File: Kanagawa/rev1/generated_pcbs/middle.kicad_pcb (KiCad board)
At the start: 2 copper layers, 330 x 142 mm, 184 parts, among them J1 Conn_01x04, SW99 Rotary_Encoder_Switch, U0 Elite-C

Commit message: edit arc for edge cut in script
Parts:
- removed MountBaseMiddleTop7: MountingHole, keyboard:MountingHole_2.2mm_M2_Pad_Via
- J1: footprint keyboard:OLED_128x64_I2C -> keyboard:OLED_128x64_I2C_cutout
- RSW0: value SW_Push -> SW_RST
- moved RSW0 57.7 mm to (312.7, 78.2)
- moved R2 35.6 mm to (364.9, 79.6)
- moved R1 29.9 mm to (362.0, 80.9)
- moved DA13 18.6 mm to (368.9, 92.9)
- moved SW99 5.53 mm to (373.8, 104.6), turned to 90 degrees
- moved J1 4.21 mm to (331.9, 79.4)
- moved MountBaseMiddleTop1 2.40 mm to (60.0, 81.0)
- moved MountBaseMiddleTop5 2.23 mm to (381.0, 81.0)
- moved MountBaseMiddleTop3 2.00 mm to (244.9, 81.2)
- moved MountMiddle0 2.00 mm to (220.9, 83.2)
- moved MountBaseMiddleTop2 0.92 mm to (60.0, 207.0)
- moved MountBaseMiddleTop4 0.92 mm to (244.0, 207.0)
- moved MountBaseMiddleTop6 0.92 mm to (380.0, 207.0)
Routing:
- net ENCA: track 39.4 -> 14.4 mm
- net RESET: track 52.6 -> 71.1 mm
- net ENCB: track 41.8 -> 27.8 mm
- net col13: track 145.1 -> 153.3 mm
- net VCC: track 76.7 -> 69.8 mm, vias 1 -> 2
- net row00: track 416.4 -> 422.5 mm, vias 0 -> 1
- net SCL: track 78.9 -> 73.7 mm
- net SDA: track 69.4 -> 66.3 mm
- net /SW99B: track 8.86 -> 10.9 mm
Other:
- board size 330 x 142 mm -> 330 x 144 mm

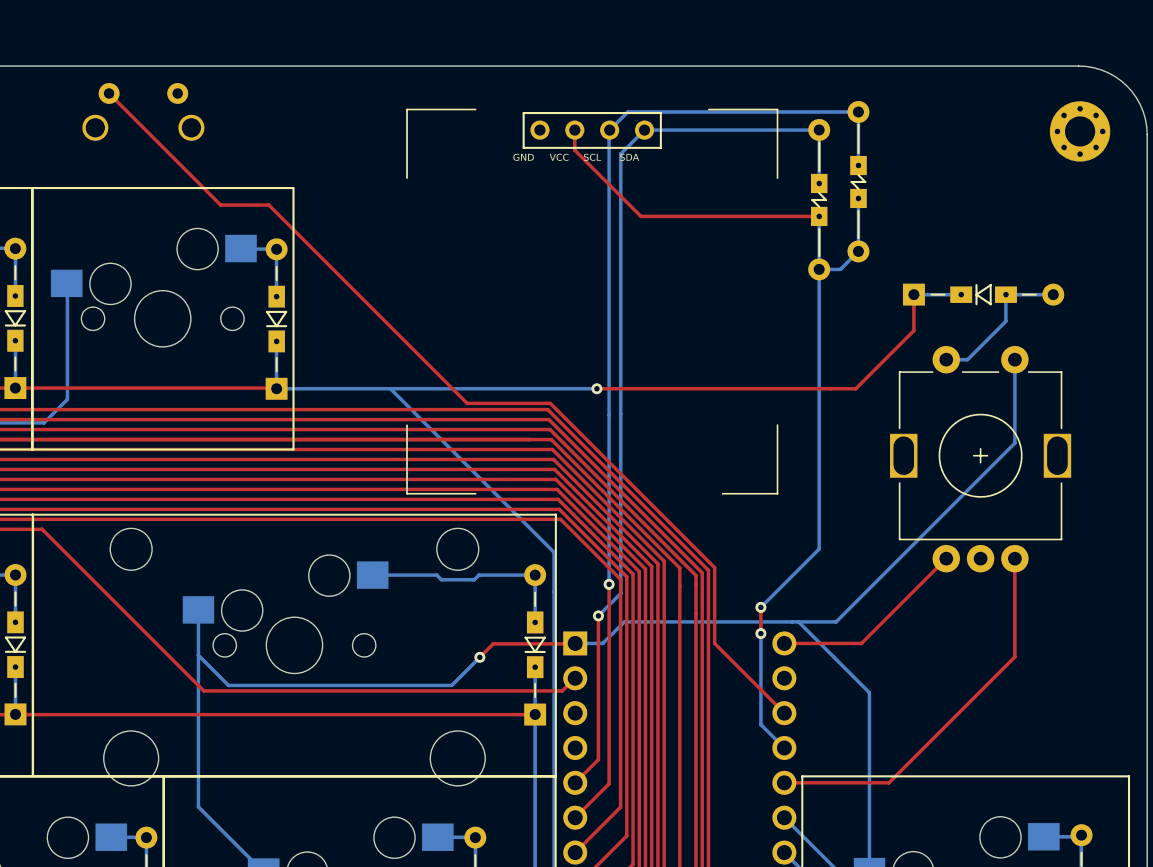
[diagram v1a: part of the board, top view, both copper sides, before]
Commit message: update script pcb generation
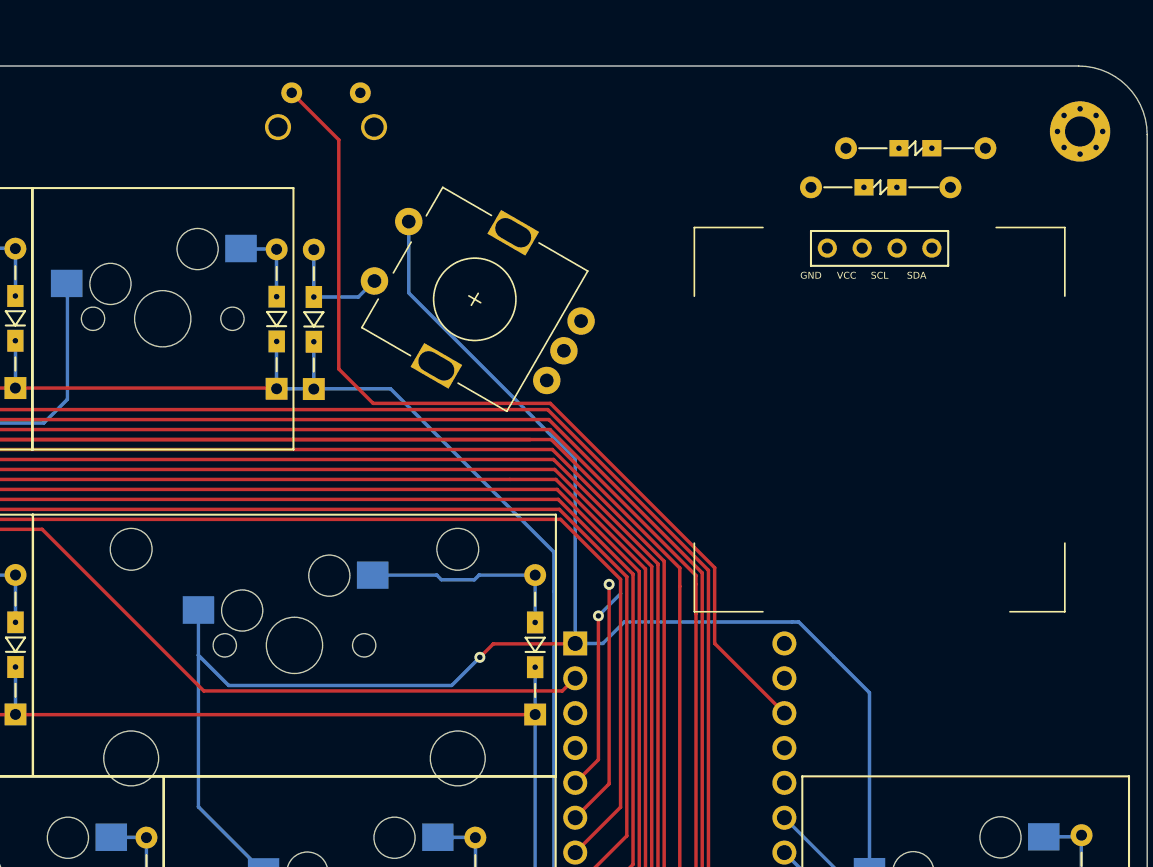
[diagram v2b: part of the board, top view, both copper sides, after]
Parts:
- moved DA13 44.3 mm to (325.2, 99.8), turned to 90 degrees
- moved SW99 38.6 mm to (336.9, 93.2), turned to 150 degrees
- moved J1 22.6 mm to (352.9, 88.0)
- moved RSW0 13.3 mm to (326.1, 78.2)
- moved R1 12.2 mm to (374.1, 82.2), turned to 180 degrees
- moved R2 8.66 mm to (371.6, 85.1), turned to 180 degrees
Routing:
- net VCC: track 69.8 -> 0.09 mm, vias 2 -> 0
- net SCL: track 73.7 -> 18.0 mm
- net SDA: track 66.3 -> 15.2 mm
- net row00: track 422.5 -> 380.0 mm, vias 1 -> 0
- net ENCB: track 27.8 -> 0.00 mm
- net ENCA: track 14.4 -> 0.00 mm
- net col13: track 153.3 -> 161.8 mm
- net RESET: track 71.1 -> 67.6 mm
- net /SW99B: track 10.9 -> 8.35 mm

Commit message: rework rev1 from fusion layout
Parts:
- added MountBaseMiddleTop3: MountingHole, keyboard:MountingHole_2.2mm_M2_Pad_Via, F.Cu at (125.9, 81.2)
- added MountBaseMiddleTop4: MountingHole, keyboard:MountingHole_2.2mm_M2_Pad_Via, F.Cu at (125.9, 207.2)
- DA0, DA1, DA10, DA11, DA12, DA13, DA2, DA3, DA4, DA5, DA6, DA7, DA8, DA9, DB0, DB1, DB10, DB11, DB12, DB13, DB2, DB3, DB4, DB5, DB6, DB7, DB8, DB9, DC0, DC1, DC10, DC11, DC12, DC13, DC2, DC3, DC4, DC5, DC6, DC7, DC8, DC9, DD0, DD1, DD10, DD11, DD12, DD13, DD2, DD3, DD4, DD5, DD6, DD7, DD8, DD9, DE0, DE1, DE10, DE11, DE12, DE13, DE2, DE3, DE4, DE5, DE6, DE7, DE8, DE9, DF0, DF1, DF10, DF11, DF12, DF13, DF2, DF3, DF4, DF5, DF6, DF7, DF8, DF9: footprint keyboard:Diode_SMD_THT -> keyboard:Diode_THT
- KD13, KE13, KF13: footprint keyboard:SW_Cherry_MX_1.25u_Hotswap -> keyboard:SW_Cherry_MX_1.00u_Hotswap
- R1, R2: footprint keyboard:Resistors_SMD_THT -> keyboard:Resistors_THT
- RSW0: value SW_RST -> SW_Push
- moved DA13 39.5 mm to (364.6, 103.2), turned to 0 degrees
- moved SW99 39.4 mm to (370.6, 113.5), turned to 90 degrees
- moved J1 22.9 mm to (331.6, 79.5)
- moved R1 17.8 mm to (364.3, 97.1), turned to 90 degrees
- moved R2 15.7 mm to (361.6, 97.1), turned to 90 degrees
- moved MountBaseMiddleTop7 4.12 mm to (376.9, 81.2)
- moved DE13 3.50 mm to (380.3, 164.9)
- moved DD13 3.48 mm to (380.3, 145.8)
- moved DF13 3.27 mm to (380.3, 184.0)
- moved MountBaseMiddleTop8 3.12 mm to (376.9, 207.2)
- moved LogoMiddle 2.83 mm to (374.9, 197.2)
- moved RSW0 2.00 mm to (324.1, 78.2)
- moved MountBaseMiddleTop1 1.90 mm to (61.9, 81.2)
- moved MountBaseMiddleTop2 1.90 mm to (61.9, 207.2)
- moved MountMiddle0 1.05 mm to (220.9, 82.2)
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- renumbered MountBaseMiddleTop3 to MountBaseMiddleTop5, MountBaseMiddleTop4 to MountBaseMiddleTop6, MountBaseMiddleTop5 to MountBaseMiddleTop7, MountBaseMiddleTop6 to MountBaseMiddleTop8
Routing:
- net VCC: track 0.09 -> 65.6 mm
- net row01: track 366.7 -> 318.3 mm
- net row02: track 353.3 -> 305.0 mm
- net SDA: track 15.2 -> 62.2 mm, vias 1 -> 2
- net row05: track 431.7 -> 386.1 mm
- net SCL: track 18.0 -> 63.5 mm, vias 1 -> 2
- net row03: track 367.3 -> 323.2 mm
- net row04: track 384.1 -> 340.3 mm
- net row00: track 380.0 -> 362.1 mm
- net ENCA: track 0.00 -> 9.82 mm, vias 0 -> 1
- net ENCB: track 0.00 -> 9.45 mm
- net col13: track 161.8 -> 155.0 mm
- net Net-(DD13-Pad2): track 6.04 -> 9.79 mm
- net Net-(DE13-Pad2): track 6.12 -> 9.79 mm
- net Net-(DF4-Pad2): track 15.5 -> 12.1 mm
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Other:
- board size 330 x 144 mm -> 325 x 143 mm

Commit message: review board
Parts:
- moved KD12 23.5 mm to (299.8, 147.3)
- moved KE0 23.4 mm to (56.9, 166.4)
- moved KF4 21.6 mm to (147.4, 190.8)
- moved KB13 21.3 mm to (304.5, 109.2)
- moved KF5 21.1 mm to (186.5, 200.6)
- moved KE11 19.2 mm to (290.3, 166.4)
- moved KD0 19.1 mm to (56.9, 147.3)
- moved KC13 17.2 mm to (314.1, 128.3)
- moved KC0 17.1 mm to (56.9, 128.3)
- moved KF2 15.2 mm to (99.8, 185.4)
- moved KF0 15.2 mm to (56.9, 185.4)
- moved KD13 13.7 mm to (381.9, 128.3)
- moved KE13 13.6 mm to (381.9, 147.3)
- moved KF13 13.6 mm to (381.9, 166.4)
- moved KA0 13.6 mm to (56.9, 85.1)
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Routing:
- net col03: track 602.9 -> 390.8 mm
- net ENCB: track 9.45 -> 19.6 mm
- net col07: track 324.4 -> 334.5 mm
- net col06: track 346.3 -> 356.4 mm
- net col08: track 303.5 -> 312.3 mm
- net col09: track 283.7 -> 290.4 mm
- net col05: track 366.8 -> 373.4 mm
- net col02: track 411.3 -> 415.6 mm
- net col01: track 441.3 -> 437.8 mm
- net col04: track 370.9 -> 372.9 mm
- net Net-(DD12-Pad2): track 14.4 -> 12.4 mm
- net col12: track 208.1 -> 209.7 mm
- net col11: track 249.9 -> 251.4 mm
- net row03: track 323.2 -> 321.7 mm
- net col13: track 155.0 -> 156.3 mm
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
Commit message: generate kanagawa gerber
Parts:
- moved RSW0 5.00 mm to (319.1, 78.2)
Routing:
- net RESET: track 68.5 -> 70.6 mm
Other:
- outline, holes or cut-outs redrawn
- board text added: "Kanagawa by Ciaanh - rev1"
- board text removed: "Kanagawa by Ciaanh - rev1 *prototype*"
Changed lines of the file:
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@@
-(kicad_pcb (version 20171130) (host pcbnew 5.1.10-88a1d61d58~90~ubuntu20.04.1)
+(kicad_pcb (version 20171130) (host pcbnew "(5.1.10)-1")
   (general
     (thickness 1.6)
-    (drawings 13)
+    (drawings 24)
     (tracks 699)
     (zones 0)
@@
     (34 B.Paste user)
     (35 F.Paste user)
-    (36 B.SilkS user hide)
+    (36 B.SilkS user)
     (37 F.SilkS user)
     (38 B.Mask user)
@@
   )
   (module keyboard:SW_RST (layer F.Cu)
-    (at 324.05 78.182)
+    (at 319.05 78.182)
     (fp_text reference RSW0 (at 0 -1.27) (layer Dwgs.User) hide
       (effects (font (size 1 1) (thickness 0.15)))
@@
       (xy 2.996029 1.227264) (xy 3.044593 1.230575) (xy 3.095505 1.230604) (xy 3.146737 1.227413)) (layer B.Mask) (width 0.01))
   )
-  (gr_text "Kanagawa by Ciaanh - rev1 *prototype*" (at 88.89 207.882) (layer B.SilkS)
+  (gr_circle (center 125.89 81.232) (end 126.99 81.232) (layer Edge.Cuts) (width 0.05))
+  (gr_circle (center 229.7994 79.8039) (end 231.3994 79.8039) (layer Edge.Cuts) (width 0.05))
+  (gr_circle (center 376.89 81.232001) (end 377.99 81.232001) (layer Edge.Cuts) (width 0.05))
+  (gr_circle (center 244.89 81.232) (end 245.99 81.232) (layer Edge.Cuts) (width 0.05))
+  (gr_circle (center 61.89 81.232) (end 62.99 81.232) (layer Edge.Cuts) (width 0.05))
+  (gr_circle (center 376.89 207.232149) (end 377.99 207.232149) (layer Edge.Cuts) (width 0.05))
+  (gr_circle (center 244.89 207.232) (end 245.99 207.232) (layer Edge.Cuts) (width 0.05))
+  (gr_circle (center 61.89 207.232) (end 62.99 207.232) (layer Edge.Cuts) (width 0.05))
+  (gr_line (start 174.178012 219.232) (end 196.489483 219.232) (layer Edge.Cuts) (width 0.05))
+  (gr_circle (center 211.94 79.8039) (end 213.54 79.8039) (layer Edge.Cuts) (width 0.05))
+  (gr_line (start 196.489483 219.232) (end 222.613839 212.232) (layer Edge.Cuts) (width 0.05))
+  (gr_line (start 376.89 212.232) (end 236.7994 212.232) (layer Edge.Cuts) (width 0.05))
+  (gr_arc (start 61.89 81.232001) (end 61.89 76.232) (angle -90) (layer Edge.Cuts) (width 0.05))
+  (gr_line (start 61.89 212.232) (end 148.053656 212.232) (layer Edge.Cuts) (width 0.05))
+  (gr_line (start 236.7994 212.232) (end 222.613839 212.232) (layer Edge.Cuts) (width 0.05))
+  (gr_circle (center 125.89 207.232) (end 126.99 207.232) (layer Edge.Cuts) (width 0.05))
+  (gr_line (start 148.053656 212.232) (end 174.178012 219.232) (layer Edge.Cuts) (width 0.05))
+  (gr_text "Kanagawa by Ciaanh - rev1" (at 88.89 207.882) (layer B.SilkS)
     (effects (font (size 1.5 1.5) (thickness 0.15)) (justify mirror))
   )
-  (gr_line (start 148.89 212.232) (end 61.89 212.232) (layer Edge.Cuts) (width 0.05))
-  (gr_line (start 175.89 219.232) (end 148.89 212.232) (layer Edge.Cuts) (width 0.05))
-  (gr_line (start 194.89 219.232) (end 175.89 219.232) (layer Edge.Cuts) (width 0.05))
-  (gr_line (start 221.89 212.232) (end 194.89 219.232) (layer Edge.Cuts) (width 0.05))
-  (gr_line (start 376.89 212.232) (end 221.89 212.232) (layer Edge.Cuts) (width 0.05))
   (gr_arc (start 376.89 81.232) (end 381.89 81.232) (angle -90) (layer Edge.Cuts) (width 0.05))
-  (gr_arc (start 61.89 81.232) (end 61.89 76.232) (angle -90) (layer Edge.Cuts) (width 0.05))
   (gr_arc (start 61.89 207.232) (end 56.89 207.232) (angle -90) (layer Edge.Cuts) (width 0.05))
   (gr_arc (start 376.89 207.232) (end 376.89 212.232) (angle -90) (layer Edge.Cuts) (width 0.05))
@@
   (segment (start 316.589999 119.212001) (end 316.589999 125.791999) (width 0.254) (layer B.Cu) (net 110))
   (segment (start 316.589999 116.183999) (end 316.589999 119.212001) (width 0.254) (layer B.Cu) (net 110))
-  (segment (start 324.98 81.612) (end 321.55 78.182) (width 0.254) (layer F.Cu) (net 111) (status 20))
   (segment (start 329.41399 100.81599) (end 324.98 96.382) (width 0.254) (layer F.Cu) (net 111))
   (segment (start 342.394914 100.81599) (end 329.41399 100.81599) (width 0.254) (layer F.Cu) (net 111))
@@
   (segment (start 359.45 123.39) (end 354.37203 118.31203) (width 0.254) (layer F.Cu) (net 111))
   (segment (start 354.37203 118.31203) (end 354.37203 112.793106) (width 0.254) (layer F.Cu) (net 111))
-  (segment (start 324.98 96.382) (end 324.98 81.612) (width 0.254) (layer F.Cu) (net 111))
+  (segment (start 324.98 96.382) (end 324.98 86.602) (width 0.254) (layer F.Cu) (net 111))
+  (segment (start 324.98 86.602) (end 316.56 78.182) (width 0.254) (layer F.Cu) (net 111))
   (zone (net 89) (net_name GND) (layer B.Cu) (hatch edge 0.508)
     (connect_pads (clearance 0.508))
